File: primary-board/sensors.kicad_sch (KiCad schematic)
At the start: 26 parts, among them J5 I2C Breakout, Q1 SFH 313 FA-3/4, Q2 SFH 313 FA-3/4, Q3 SFH 313 FA-3/4, Q4 SFH 313 FA-3/4, Q5 NMOS, Q6 NMOS, Q7 NMOS, Q8 NMOS, U6 TLV9004xRUCR

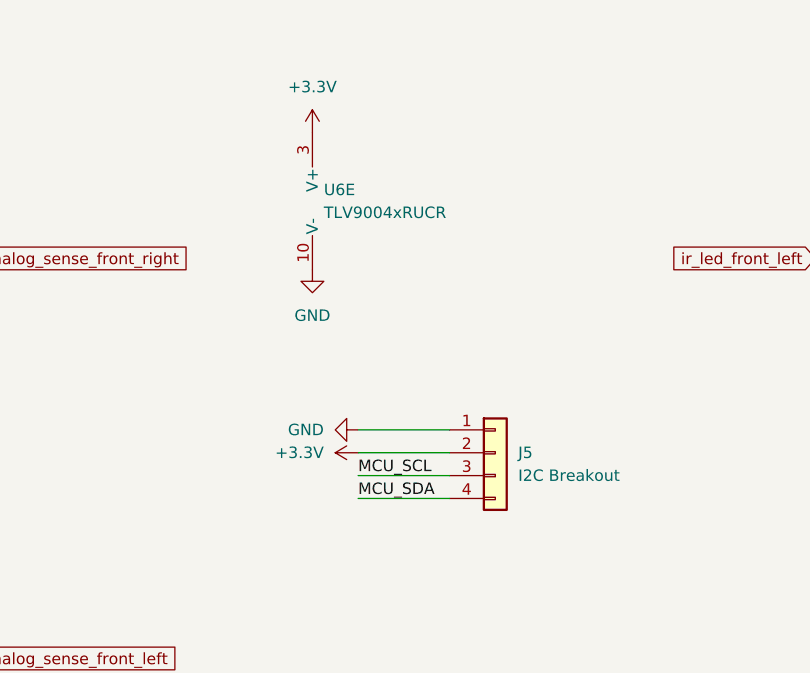
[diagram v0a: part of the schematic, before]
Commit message: routed analog sensors
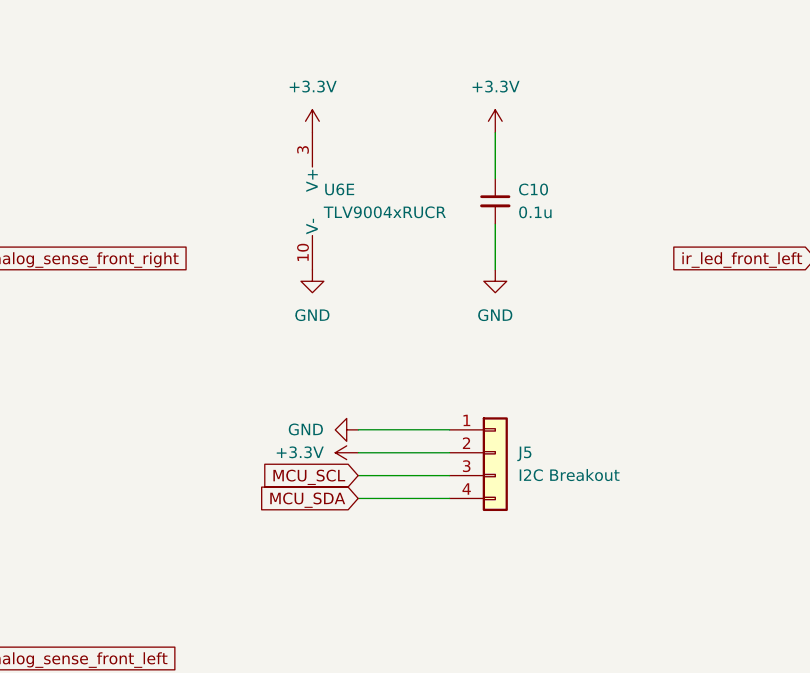
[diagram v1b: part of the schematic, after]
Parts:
- added C10: 0.1u, Capacitor_SMD:C_0603_1608Metric, symbol Device:C_Small
- D1, D2, D5, D6: footprint (none) -> LED_THT:LED_D5.0mm_IRGrey
- Q1, Q2, Q3, Q4: footprint SFH 313 FA-3/4_OSR -> LED_THT:LED_D5.0mm_IRGrey
- Q5, Q6, Q7, Q8: footprint (none) -> Package_TO_SOT_SMD:SOT-23-3
- R12, R13, R14, R15, R16, R17, R18, R19, R20, R21, R22, R3: footprint (none) -> Resistor_SMD:R_0603_1608Metric
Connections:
- net +3.3V: now also C10.1
- net GND: now also C10.2
